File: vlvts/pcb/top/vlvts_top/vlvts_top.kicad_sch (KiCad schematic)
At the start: 3 parts, among them J2 Conn_01x14_Male

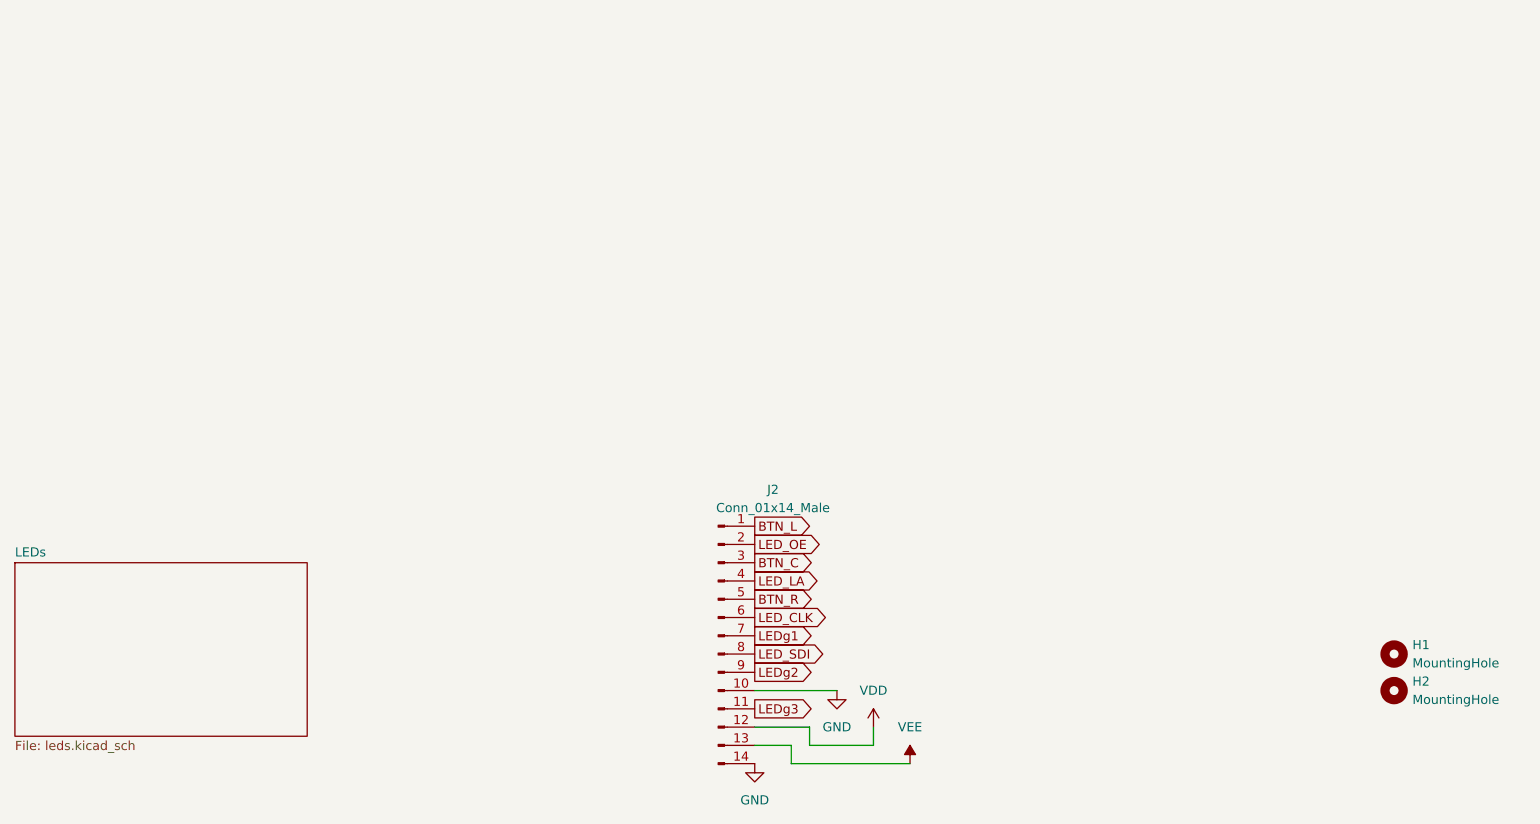
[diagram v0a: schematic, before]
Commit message: vlvts: new pcb
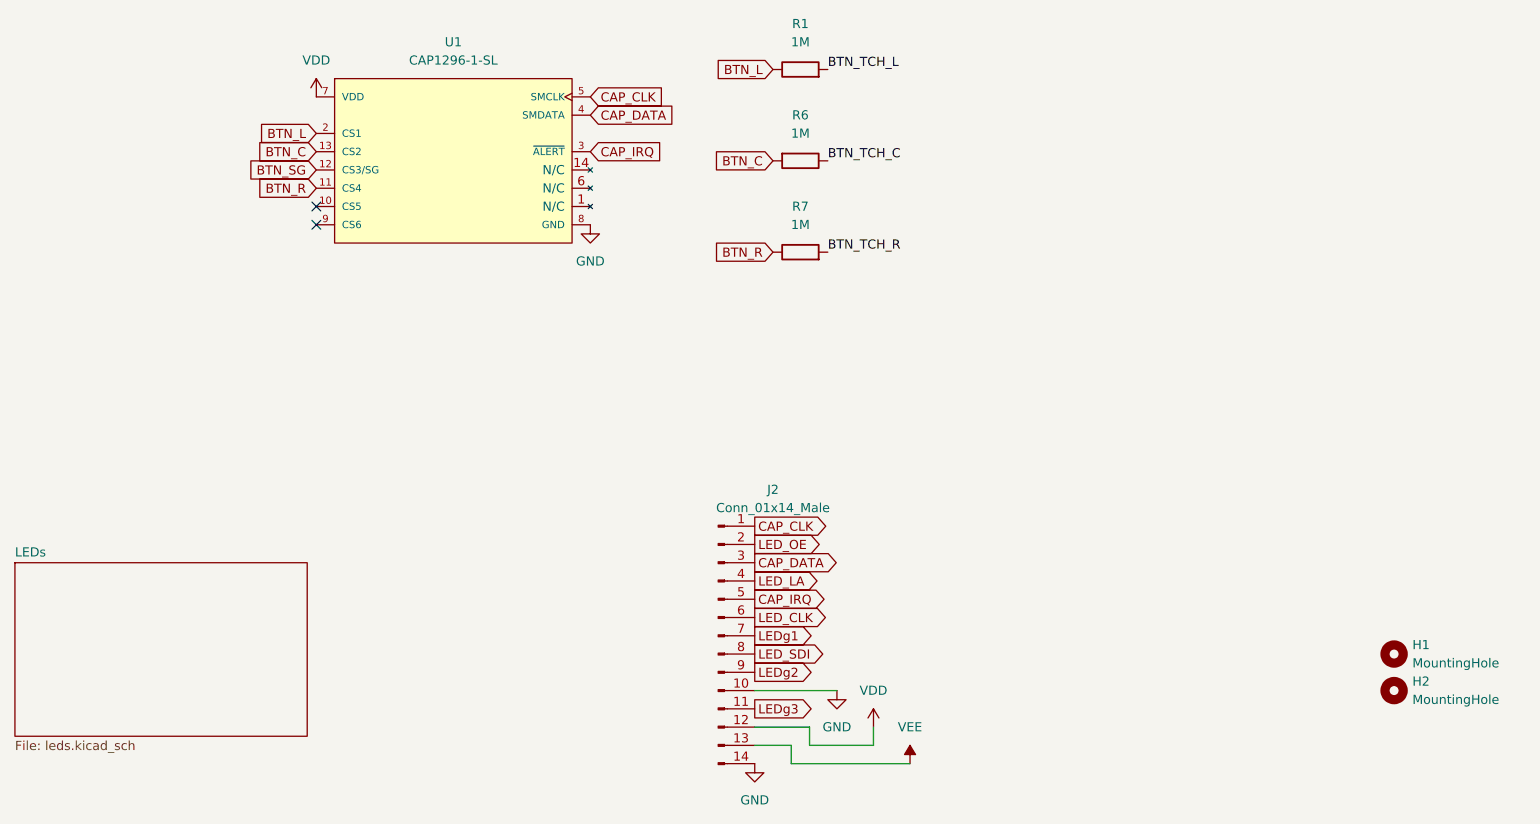
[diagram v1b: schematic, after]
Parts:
- added R1, R6, R7: 1M, Resistor_SMD:R_0603_1608Metric_Pad0.98x0.95mm_HandSolder, symbol Device:R
- added U1: CAP1296-1-SL, Package_SO:SOIC-14_3.9x8.7mm_P1.27mm, symbol cap_tch:CAP1296-1-SL
- H1, H2: footprint MountingHole:MountingHole_2.5mm -> MountingHole:MountingHole_3.2mm_M3_DIN965
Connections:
- net BTN_C: now also R6.2, U1.13 (CS2); no longer J2.3 (Pin_3)
- net BTN_L: now also R1.1, U1.2 (CS1); no longer J2.1 (Pin_1)
- net BTN_R: now also R7.1, U1.11 (CS4); no longer J2.5 (Pin_5)
- net GND: now also U1.8 (GND)
- net VDD: now also U1.7 (VDD)
- new net BTN_SG: U1.12 (CS3/SG)
- new net BTN_TCH_C: R6.1
- new net BTN_TCH_L: R1.2
- new net BTN_TCH_R: R7.2
- new net CAP_CLK: J2.1 (Pin_1), U1.5 (SMCLK)
- new net CAP_DATA: J2.3 (Pin_3), U1.4 (SMDATA)
- new net CAP_IRQ: J2.5 (Pin_5), U1.3 (~{ALERT})
- no-connect marks 0 -> 2
